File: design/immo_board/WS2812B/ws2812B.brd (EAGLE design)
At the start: 59.4 x 17.8 mm, 11 parts

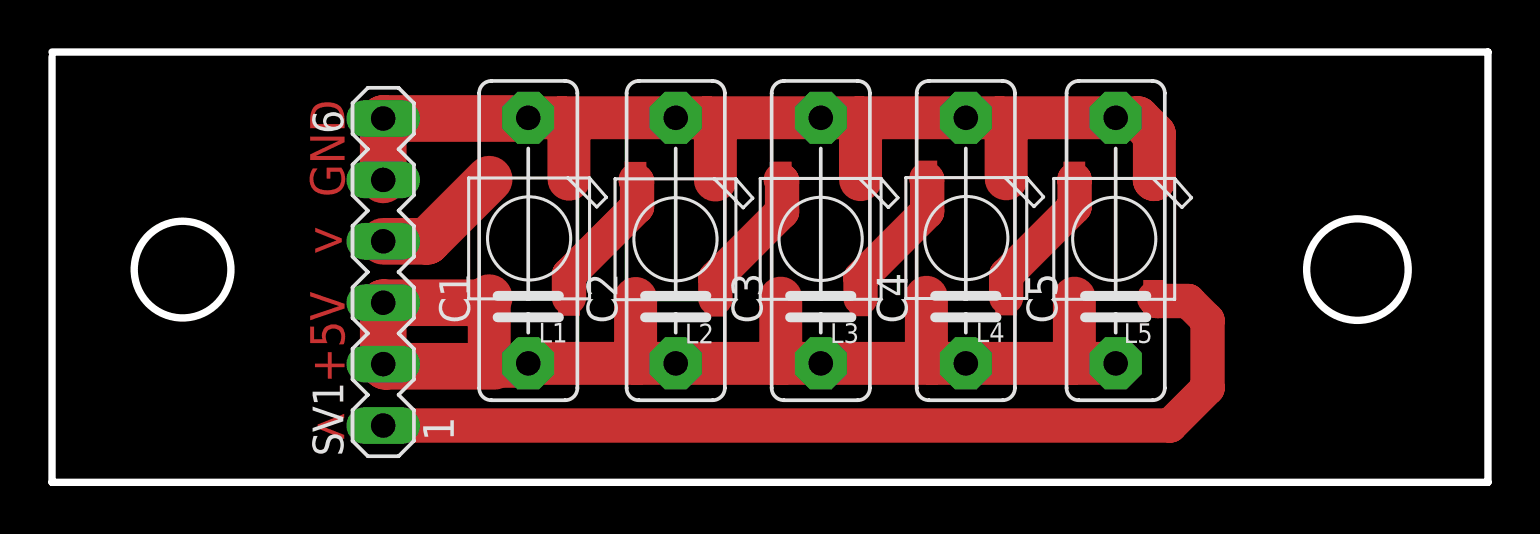
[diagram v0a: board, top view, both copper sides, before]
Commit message: Fix board and electric scheme. Add capacitors.
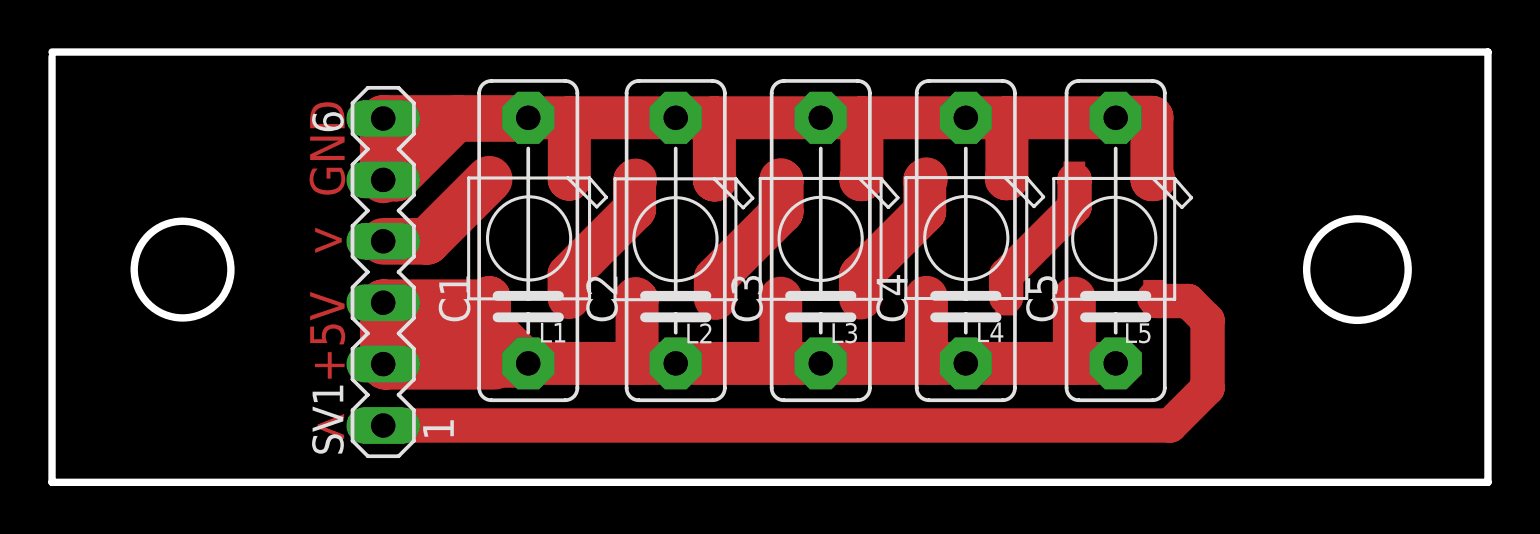
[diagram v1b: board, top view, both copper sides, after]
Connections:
- net VCC renamed +5V
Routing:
- net +5V: track 51.3 -> 65.4 mm
- net GND: track 47.2 -> 51.5 mm
